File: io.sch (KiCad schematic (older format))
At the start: 18 parts, among them P1 CONN_01X03, P2 CONN_01X03, P3 CONN_01X03, P4 CONN_01X03, X1 CON-JST_SM04B-SRSS-TB, X2 CON-JST_SM04B-SRSS-TB, X3 CON-JST_SM04B-SRSS-TB, X4 CON-JST_SM04B-SRSS-TB, X5 CON-JST_SM04B-SRSS-TB, X7 CON-JST_SM04B-SRSS-TB, X8 CON-JST_SM04B-SRSS-TB

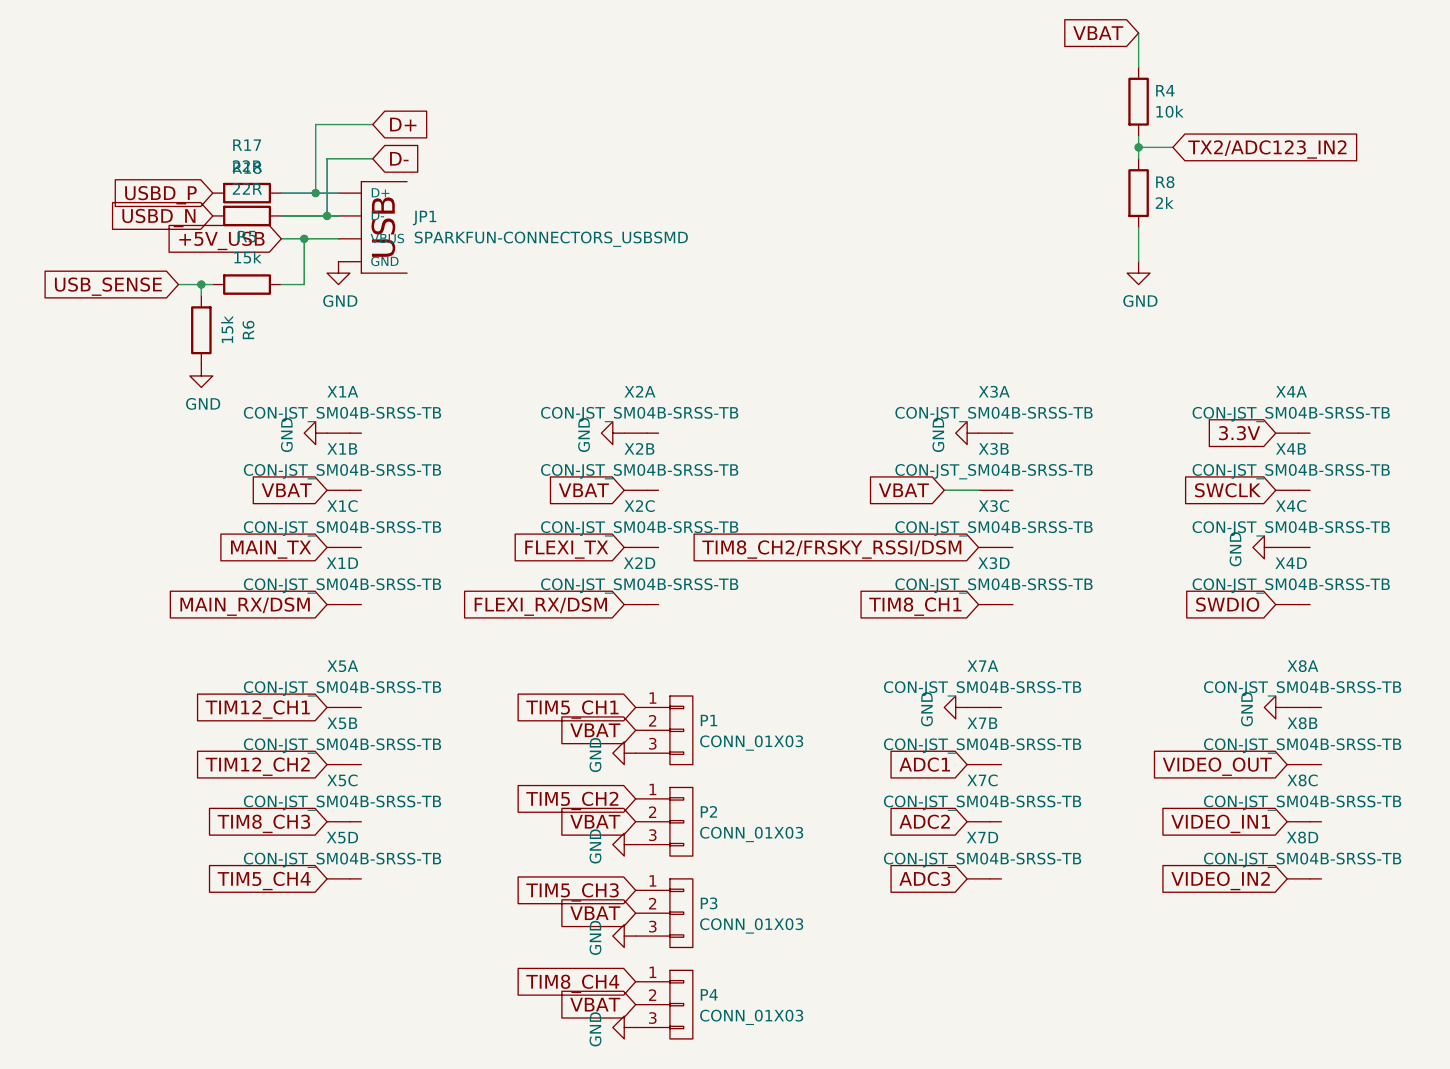
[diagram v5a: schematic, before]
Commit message: power traces routed
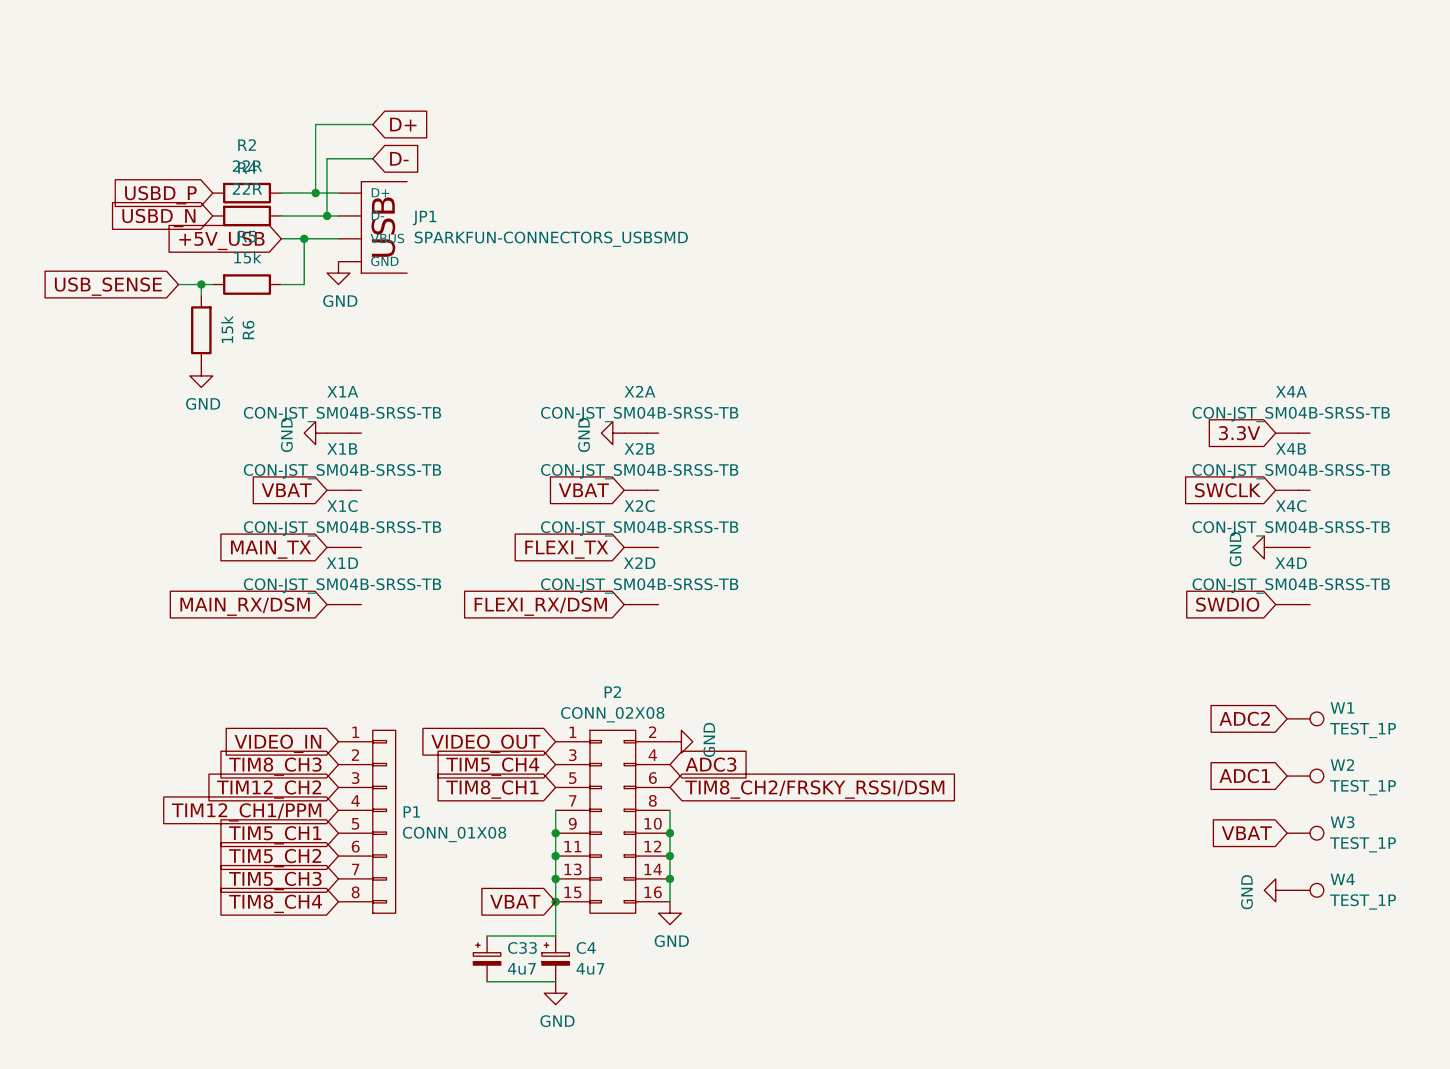
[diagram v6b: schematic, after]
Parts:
- removed P1, P2, P3, P4: CONN_01X03, Pin_Headers:Pin_Header_Angled_1x03, symbol CONN_01X03
- removed R4: 10k, Resistors_SMD:R_0402, symbol R
- removed R8: 2k, Resistors_SMD:R_0402, symbol R
- removed X3, X5, X7, X8: CON-JST_SM04B-SRSS-TB, Connectors_JST_SH:Connectors_JST_SM04B-SRSS-TB, symbol CON-JST_SM04B-SRSS-TB
- added C33, C4: 4u7, Capacitors_Tantalum_SMD:TantalC_SizeA_EIA-3216_Reflow, symbol CP_Small
- added P1: CONN_01X08, Pin_Headers:Pin_Header_Straight_1x08, symbol CONN_01X08
- added P2: CONN_02X08, Pin_Headers:Pin_Header_Straight_2x08, symbol CONN_02X08
- added W1, W2, W3, W4: TEST_1P, Measurement_Points:Measurement_Point_Square-SMD-Pad_Big, symbol TEST_1P
- R2: renamed from R17; footprint Resistors_SMD:R_0402 -> Resistors_SMD:R_0603
- R4: renamed from R18; footprint Resistors_SMD:R_0402 -> Resistors_SMD:R_0603
- R5, R6: footprint Resistors_SMD:R_0402 -> Resistors_SMD:R_0603
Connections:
- net ADC1: now also W2.1
- net ADC2: now also W1.1
- net ADC3: now also P2.4 (P4)
- net GND: now also C33.2, C4.2, P2.10 (P10), P2.12 (P12), P2.14 (P14), P2.16 (P16), P2.2 (P2), P2.8 (P8), W4.1
- net TIM12_CH2: now also P1.3 (P3)
- net TIM5_CH1: now also P1.5 (P5)
- net TIM5_CH2: now also P1.6 (P6)
- net TIM5_CH3: now also P1.7 (P7)
- net TIM5_CH4: now also P2.3 (P3)
- net TIM8_CH1: now also P2.5 (P5)
- net TIM8_CH2/FRSKY_RSSI/DSM: now also P2.6 (P6)
- net TIM8_CH3: now also P1.2 (P2)
- net TIM8_CH4: now also P1.8 (P8)
- net VBAT: now also C33.1, C4.1, P2.11 (P11), P2.13 (P13), P2.15 (P15), P2.7 (P7), P2.9 (P9), W3.1
- net VIDEO_OUT: now also P2.1 (P1)
- new net TIM12_CH1/PPM: P1.4 (P4)
- new net VIDEO_IN: P1.1 (P1)

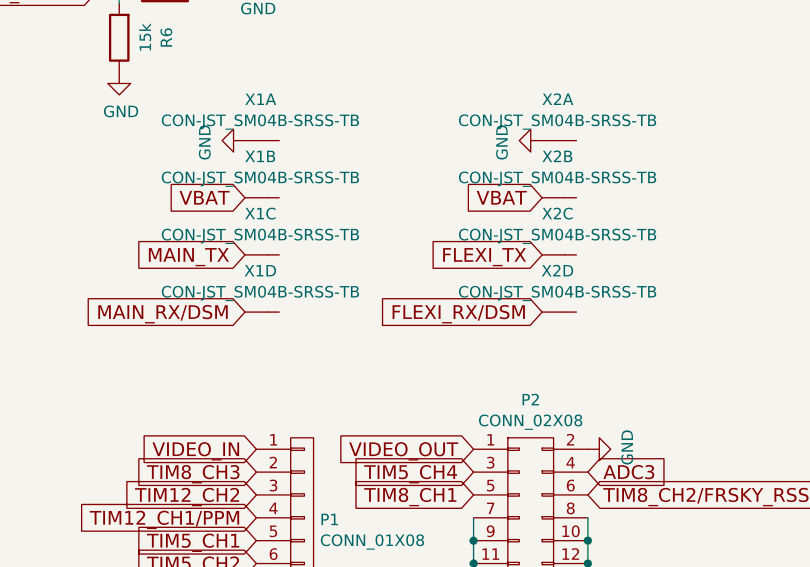
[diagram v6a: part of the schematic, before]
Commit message: best relative placement
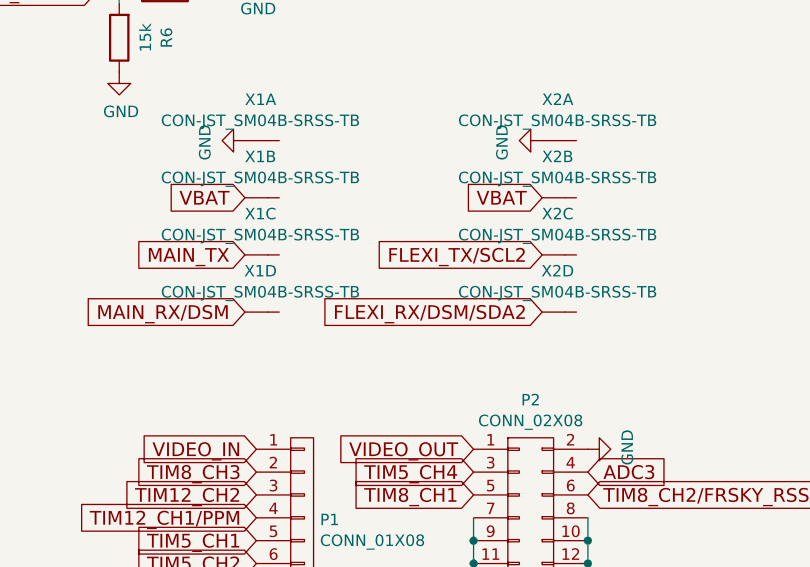
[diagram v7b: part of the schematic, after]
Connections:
- net FLEXI_RX/DSM renamed FLEXI_RX/DSM/SDA2
- net FLEXI_TX renamed FLEXI_TX/SCL2
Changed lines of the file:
@@
 $EndComp
 Text GLabel 4800 3600 0    60   Input ~ 0
-FLEXI_RX/DSM
+FLEXI_RX/DSM/SDA2
 Text GLabel 4800 3350 0    60   Input ~ 0
-FLEXI_TX
+FLEXI_TX/SCL2
 $Comp
 L GND #PWR02

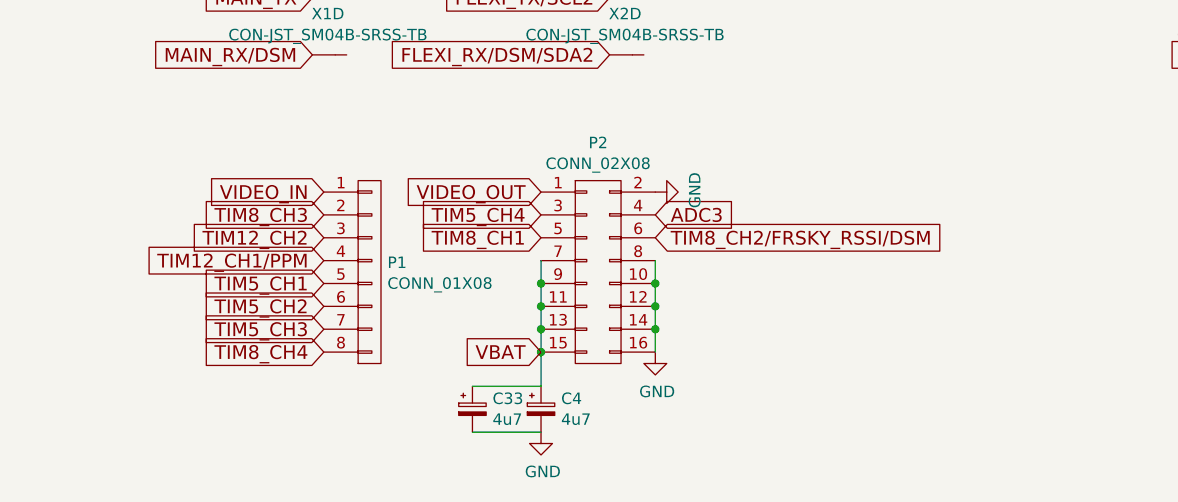
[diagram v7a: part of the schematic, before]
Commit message: first pass routing complete
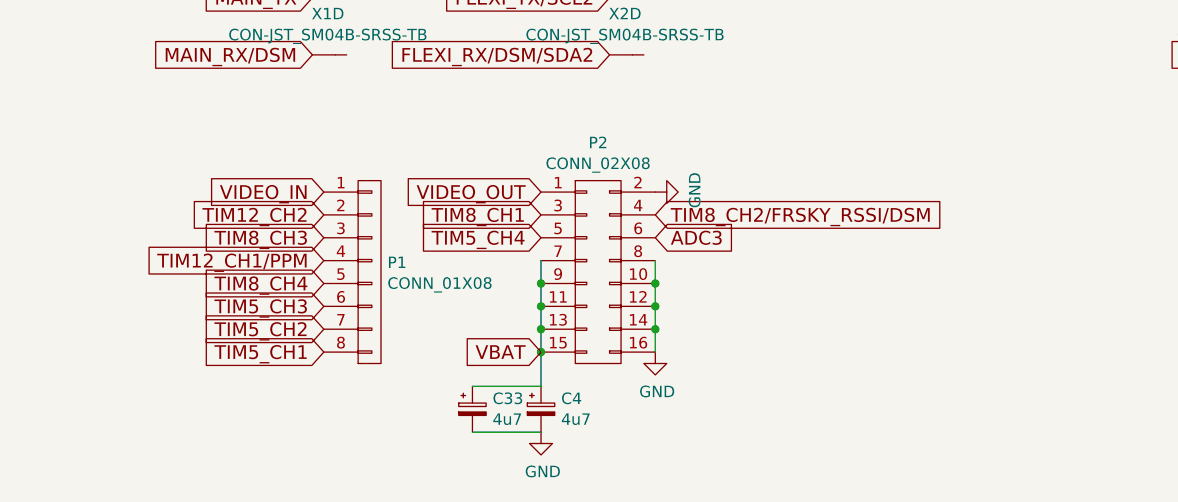
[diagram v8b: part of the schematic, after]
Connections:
- net ADC3: now also P2.6 (P6); no longer P2.4 (P4)
- net TIM12_CH2: now also P1.2 (P2); no longer P1.3 (P3)
- net TIM5_CH1: now also P1.8 (P8); no longer P1.5 (P5)
- net TIM5_CH2: now also P1.7 (P7); no longer P1.6 (P6)
- net TIM5_CH3: now also P1.6 (P6); no longer P1.7 (P7)
- net TIM5_CH4: now also P2.5 (P5); no longer P2.3 (P3)
- net TIM8_CH1: now also P2.3 (P3); no longer P2.5 (P5)
- net TIM8_CH2/FRSKY_RSSI/DSM: now also P2.4 (P4); no longer P2.6 (P6)
- net TIM8_CH3: now also P1.3 (P3); no longer P1.2 (P2)
- net TIM8_CH4: now also P1.5 (P5); no longer P1.8 (P8)
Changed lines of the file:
@@
 	0    -1   -1   0
 $EndComp
+Text GLabel 3550 4600 0    60   Input ~ 0
+TIM8_CH4
+Text GLabel 3550 4700 0    60   Input ~ 0
+TIM5_CH3
+Text GLabel 3550 4800 0    60   Input ~ 0
+TIM5_CH2
 Text GLabel 3550 4900 0    60   Input ~ 0
-TIM8_CH4
-Text GLabel 3550 4800 0    60   Input ~ 0
-TIM5_CH3
-Text GLabel 3550 4700 0    60   Input ~ 0
-TIM5_CH2
-Text GLabel 3550 4600 0    60   Input ~ 0
 TIM5_CH1
 Text GLabel 3550 4200 0    60   Input ~ 0
@@
 Text GLabel 3550 4500 0    60   Input ~ 0
 TIM12_CH1/PPM
+Text GLabel 5000 4300 2    60   Input ~ 0
+TIM8_CH2/FRSKY_RSSI/DSM
+Text GLabel 3550 4300 0    60   Input ~ 0
+TIM12_CH2
+Text GLabel 4500 4300 0    60   Input ~ 0
+TIM8_CH1
+Text GLabel 3550 4400 0    60   Input ~ 0
+TIM8_CH3
+Text GLabel 4500 4400 0    60   Input ~ 0
+TIM5_CH4
 Text GLabel 5000 4400 2    60   Input ~ 0
-TIM8_CH2/FRSKY_RSSI/DSM
-Text GLabel 3550 4400 0    60   Input ~ 0
-TIM12_CH2
-Text GLabel 4500 4400 0    60   Input ~ 0
-TIM8_CH1
-Text GLabel 3550 4300 0    60   Input ~ 0
-TIM8_CH3
-Text GLabel 4500 4300 0    60   Input ~ 0
-TIM5_CH4
-Text GLabel 5000 4300 2    60   Input ~ 0
 ADC3
 $Comp
